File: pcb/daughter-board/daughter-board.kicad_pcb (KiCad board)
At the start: 2 copper layers, 50 x 30 mm, 11 parts, among them J1 Conn_01x06_MountingPin, J2 USB_C_Receptacle_USB2.0_16P, J4 4P4C_Shielded, U1 SRV05-4

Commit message: schematics review with scgh
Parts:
- removed D1: D_Schottky, Diode_SMD:D_SOD-123
- added C1: 100n, Capacitor_SMD:C_0603_1608Metric, F.Cu at (127.6, 63.7)
- added R3: 220k, Resistor_SMD:R_0603_1608Metric, F.Cu at (127.6, 66.0)
- moved J4 10.9 mm to (116.5, 73.2)
- moved R2 6.96 mm to (139.2, 70.8)
- moved R1 1.39 mm to (132.8, 70.8)
- moved J2 0.52 mm to (136.0, 62.6)
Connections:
- J2 pad A4: VBUS -> +5V
- J2 pad A9: VBUS -> +5V
- J2 pad B4: VBUS -> +5V
- J2 pad B9: VBUS -> +5V
- J2 pad S1: GND -> Net-(J2-SHIELD)
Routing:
- net Net-(J2-SHIELD): track 0.00 -> 28.9 mm
- net GND: track 29.7 -> 5.93 mm, vias 3 -> 2
- net VBUS: track 11.6 -> 0.00 mm
- net +5V: track 46.4 -> 53.7 mm, vias 2 -> 4
- net /SPLIT_RX: track 25.1 -> 17.8 mm, vias 0 -> 2
- net Net-(J2-CC1): track 10.7 -> 5.10 mm, vias 2 -> 0
- net /SPLIT_TX: track 26.4 -> 22.9 mm, vias 2 -> 0
- net /USB_D-: track 29.1 -> 31.6 mm
- net Net-(J2-CC2): track 2.54 -> 4.72 mm
- net /USB_D+: track 28.9 -> 30.1 mm
- added copper zone on F.Cu, net GND

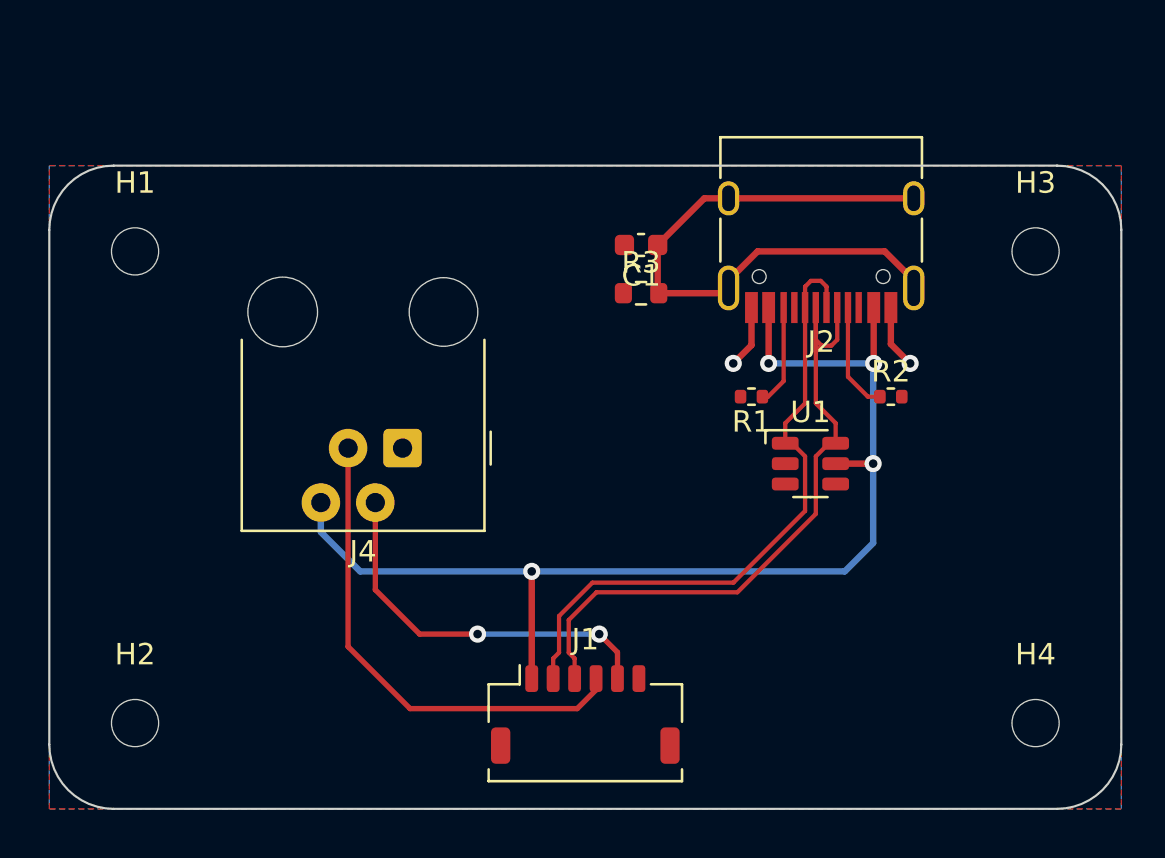
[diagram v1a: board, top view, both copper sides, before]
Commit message: layout ready for review
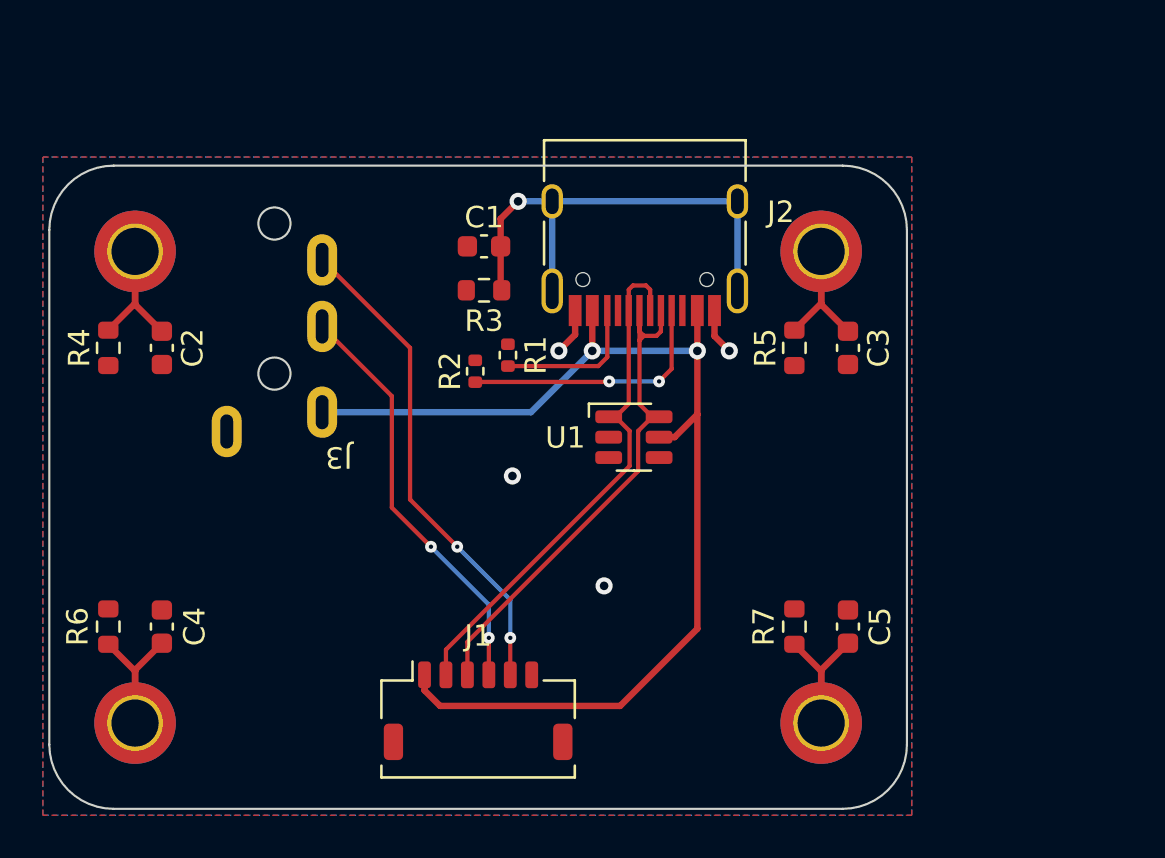
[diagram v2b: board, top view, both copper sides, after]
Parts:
- removed J4: 4P4C_Shielded, Connector_RJ:RJ9_Evercom_5301-440xxx_Horizontal
- added C2: 100n, Capacitor_SMD:C_0603_1608Metric, F.Cu at (105.2, 68.5)
- added C3: 100n, Capacitor_SMD:C_0603_1608Metric, F.Cu at (137.2, 68.5)
- added C4: 100n, Capacitor_SMD:C_0603_1608Metric, F.Cu at (105.2, 81.5)
- added C5: 100n, Capacitor_SMD:C_0603_1608Metric, F.Cu at (137.2, 81.5)
- added J3: PJ-320A, lib-zegonix:TRRS_Receptable, F.Cu at (113.5, 73.1)
- added R4: 330, Resistor_SMD:R_0603_1608Metric, F.Cu at (102.8, 68.5)
- added R5: 330, Resistor_SMD:R_0603_1608Metric, F.Cu at (134.8, 68.5)
- added R6: 330, Resistor_SMD:R_0603_1608Metric, F.Cu at (102.8, 81.5)
- added R7: 330, Resistor_SMD:R_0603_1608Metric, F.Cu at (134.8, 81.5)
- H1, H2, H3, H4: value MountingHole -> MountingHole_Pad; footprint MountingHole:MountingHole_2.2mm_M2 -> MountingHole:MountingHole_2.2mm_M2_DIN965_Pad_TopBottom
- R3: value 220k -> 330
- moved H3 47.4 mm to (104.0, 86.0)
- moved H2 38.8 mm to (136.0, 64.0)
- moved R2 19.4 mm to (119.9, 69.6), turned to 90 degrees
- moved R1 11.5 mm to (121.4, 68.8), turned to 90 degrees
- moved H4 10.0 mm to (136.0, 86.0)
- moved U1 8.33 mm to (127.3, 72.7)
- moved J2 8.23 mm to (127.8, 62.7)
- moved R3 7.33 mm to (120.3, 65.8), turned to 180 degrees
- moved C1 7.33 mm to (120.3, 63.8)
- moved J1 5.00 mm to (120.0, 85.4)
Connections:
- R3 pad 1: GND -> Net-(J2-SHIELD)
- R3 pad 2: Net-(J2-SHIELD) -> GND
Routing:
- net Net-(C5-Pad1): track 0.00 -> 8.44 mm
- net Net-(C4-Pad1): track 0.00 -> 8.44 mm
- net Net-(C3-Pad1): track 0.00 -> 8.44 mm
- net Net-(C2-Pad1): track 0.00 -> 8.44 mm
- net Net-(J2-CC1): track 5.10 -> 12.1 mm, vias 0 -> 2
- net /USB_D-: track 31.6 -> 24.9 mm
- net Net-(J2-SHIELD): track 28.9 -> 23.1 mm, vias 0 -> 1
- net /USB_D+: track 30.1 -> 24.8 mm
- net /SPLIT_RX: track 17.8 -> 23.0 mm
- net /SPLIT_TX: track 22.9 -> 19.5 mm, vias 0 -> 2
- net Net-(J2-CC2): track 4.72 -> 6.98 mm
- net GND: track 5.93 -> 4.36 mm, vias 2 -> 4
- net +5V: track 53.7 -> 52.9 mm, vias 4 -> 2
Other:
- board size 50 x 30 mm -> 40 x 30 mm
